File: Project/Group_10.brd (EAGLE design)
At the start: 73.7 x 48.3 mm, 29 parts, among them J1 POWER_JACKPTH_LOCK, U1 +12v, U3 TCA9546ASO16, U4 TMUX1208

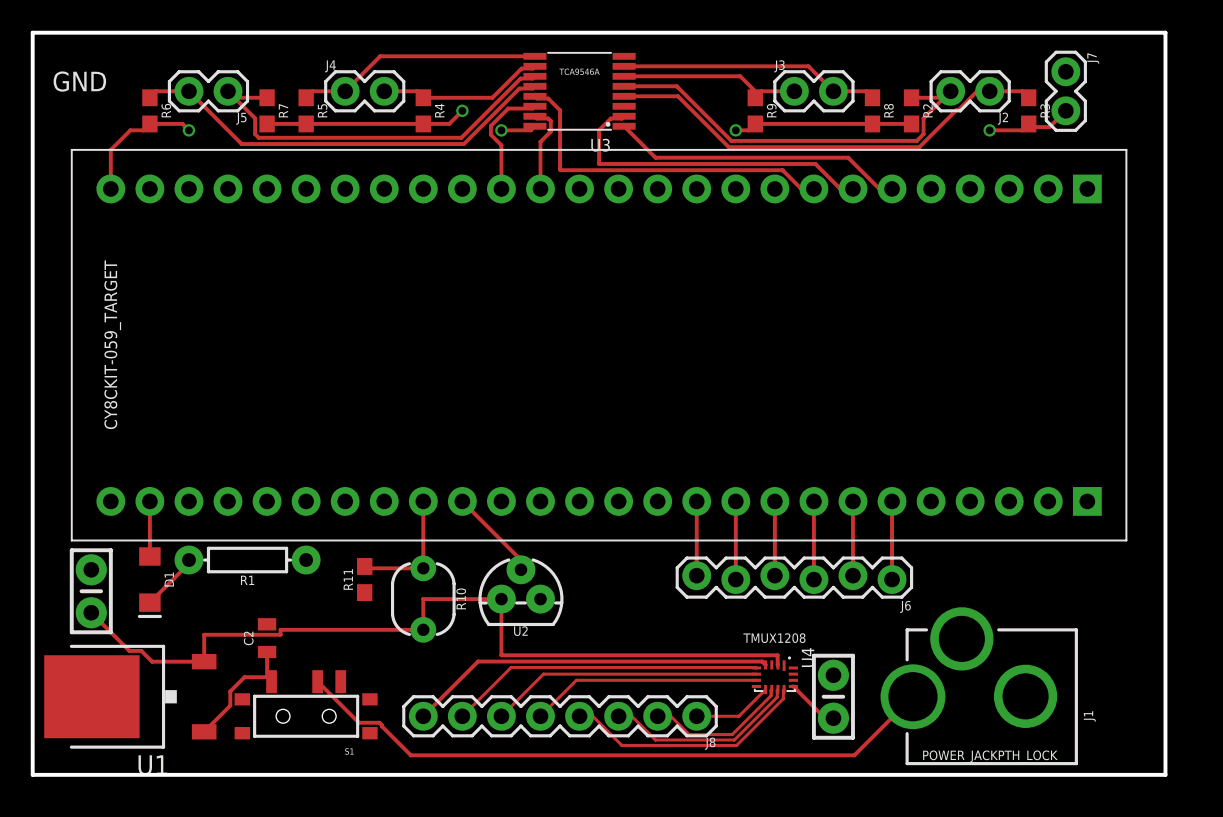
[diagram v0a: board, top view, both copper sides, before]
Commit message: Updated devices on board, corrected isolate of copper pour, simplified some routing
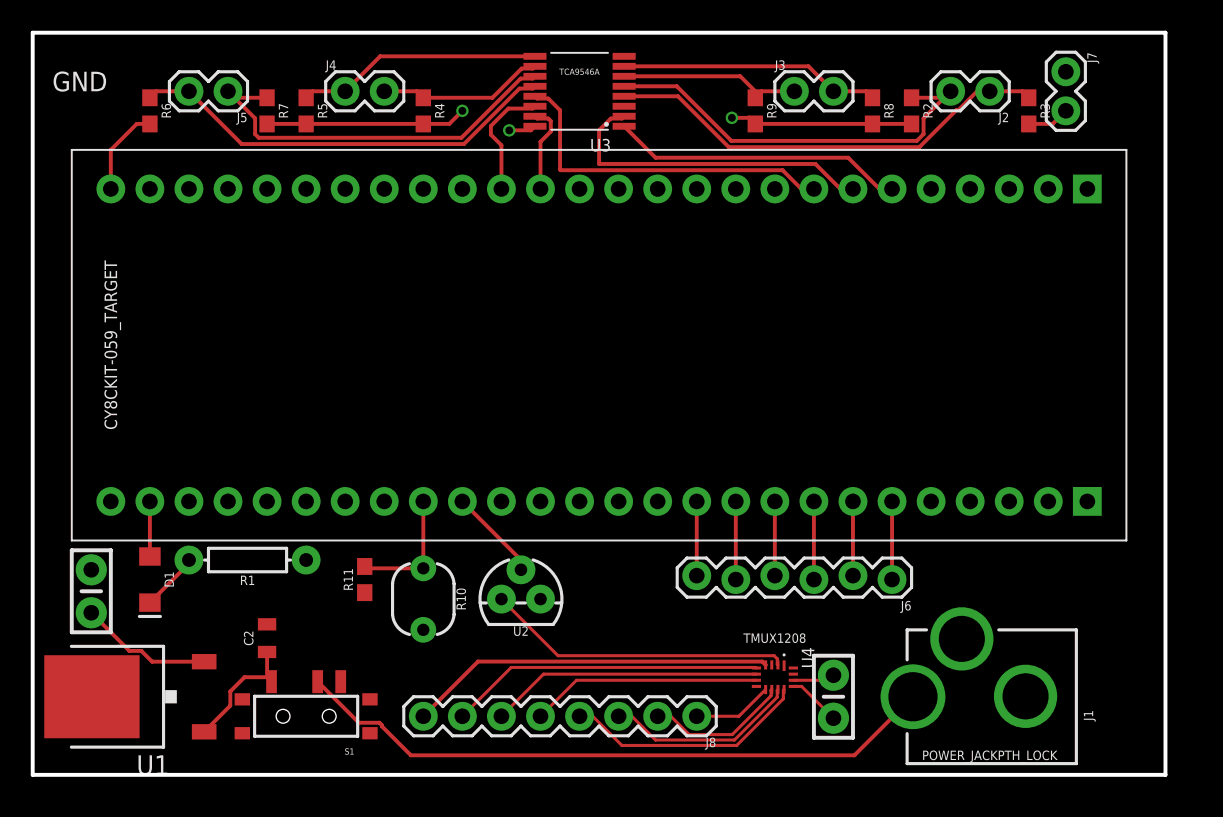
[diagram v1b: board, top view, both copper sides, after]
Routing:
- net 5V: track 99.0 -> 67.3 mm, vias 5 -> 3
- net GND: track 0.00 -> 2.75 mm
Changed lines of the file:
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@@
 <setting verticaltext="up"/>
 </settings>
-<grid distance="0.05" unitdist="inch" unit="mil" style="lines" multiple="1" display="yes" altdistance="0.005" altunitdist="inch" altunit="inch"/>
+<grid distance="2" unitdist="mil" unit="mil" style="lines" multiple="1" display="yes" altdistance="2" altunitdist="mil" altunit="mil"/>
 <layers>
 <layer number="1" name="Top" color="4" fill="1" visible="yes" active="yes"/>
@@
 <layer number="23" name="tOrigins" color="15" fill="1" visible="yes" active="yes"/>
 <layer number="24" name="bOrigins" color="15" fill="1" visible="yes" active="yes"/>
-<layer number="25" name="tNames" color="7" fill="1" visible="no" active="yes"/>
+<layer number="25" name="tNames" color="7" fill="1" visible="yes" active="yes"/>
 <layer number="26" name="bNames" color="7" fill="1" visible="no" active="yes"/>
-<layer number="27" name="tValues" color="7" fill="1" visible="no" active="yes"/>
+<layer number="27" name="tValues" color="7" fill="1" visible="yes" active="yes"/>
 <layer number="28" name="bValues" color="7" fill="1" visible="no" active="yes"/>
 <layer number="29" name="tStop" color="7" fill="3" visible="no" active="yes"/>
@@
 </class>
 </classes>
-<designrules name="Group_10">
+<designrules name="Group_10 *">
 <description language="en">Design rules from &lt;a href=&quot;https://www.mdsrl.it/&quot;&gt;MD srl&lt;/a&gt;</description>
 <param name="layerSetup" value="(1*16)"/>
@@
 <contactref element="U3" pad="3"/>
 <contactref element="U3" pad="8"/>
-<polygon width="0.254" layer="1">
+<polygon width="0.254" layer="1" isolate="0.2032">
 <vertex x="-74.93" y="45.72"/>
 <vertex x="-74.93" y="93.98"/>
@@
 <vertex x="-1.27" y="45.72"/>
 </polygon>
+<wire x1="-25.47" y1="51.87" x2="-23.187" y2="51.87" width="0.2" layer="1"/>
+<wire x1="-23.187" y1="51.87" x2="-22.86" y2="52.197" width="0.2" layer="1"/>
 </signal>
 <signal name="12V">
@@
 <contactref element="U3" pad="16"/>
 <wire x1="-42.27" y1="87.895" x2="-42.535" y2="87.63" width="0.254" layer="1"/>
-<wire x1="-42.535" y1="87.63" x2="-44.45" y2="87.63" width="0.254" layer="1"/>
-<via x="-44.45" y="87.63" extent="1-16" drill="0.508"/>
+<wire x1="-42.535" y1="87.63" x2="-43.942" y2="87.63" width="0.254" layer="1"/>
+<via x="-43.942" y="87.63" extent="1-16" drill="0.508"/>
 <wire x1="-59.69" y1="88.05" x2="-57.15" y2="88.05" width="0.254" layer="1"/>
-<wire x1="-67.31" y1="88.05" x2="-65.19" y2="88.05" width="0.254" layer="1"/>
-<wire x1="-65.19" y1="88.05" x2="-64.77" y2="87.63" width="0.254" layer="1"/>
-<via x="-64.77" y="87.63" extent="1-16" drill="0.508"/>
 <wire x1="-57.15" y1="88.05" x2="-49.53" y2="88.05" width="0.254" layer="1"/>
 <wire x1="-49.53" y1="88.05" x2="-47.84" y2="88.05" width="0.254" layer="1"/>
 <wire x1="-47.84" y1="88.05" x2="-46.99" y2="88.9" width="0.254" layer="1"/>
 <via x="-46.99" y="88.9" extent="1-16" drill="0.508"/>
-<wire x1="-67.31" y1="88.05" x2="-67.73" y2="87.63" width="0.254" layer="1"/>
-<wire x1="-67.73" y1="87.63" x2="-68.58" y2="87.63" width="0.254" layer="1"/>
-<wire x1="-68.58" y1="87.63" x2="-69.85" y2="86.36" width="0.254" layer="1"/>
-<wire x1="-69.85" y1="86.36" x2="-69.85" y2="83.82" width="0.254" layer="1"/>
-<wire x1="-27.94" y1="88.05" x2="-28.36" y2="87.63" width="0.254" layer="1"/>
-<wire x1="-28.36" y1="87.63" x2="-29.21" y2="87.63" width="0.254" layer="1"/>
-<via x="-29.21" y="87.63" extent="1-16" drill="0.508"/>
+<wire x1="-69.85" y1="83.82" x2="-69.85" y2="86.36" width="0.254" layer="1"/>
+<wire x1="-27.94" y1="88.05" x2="-28.3328" y2="88.4428" width="0.254" layer="1"/>
+<wire x1="-28.3328" y1="88.4428" x2="-29.464" y2="88.4428" width="0.254" layer="1"/>
+<via x="-29.464" y="88.4428" extent="1-16" drill="0.508"/>
 <wire x1="-27.94" y1="88.05" x2="-20.32" y2="88.05" width="0.254" layer="1"/>
 <wire x1="-20.32" y1="88.05" x2="-17.78" y2="88.05" width="0.254" layer="1"/>
-<wire x1="-10.16" y1="88.05" x2="-10.37" y2="87.84" width="0.254" layer="1"/>
-<wire x1="-10.37" y1="87.84" x2="-10.58" y2="87.63" width="0.254" layer="1"/>
-<wire x1="-10.58" y1="87.63" x2="-12.7" y2="87.63" width="0.254" layer="1"/>
-<via x="-12.7" y="87.63" extent="1-16" drill="0.508"/>
-<wire x1="-7.747" y1="88.9" x2="-8.807" y2="87.84" width="0.254" layer="1"/>
-<wire x1="-8.807" y1="87.84" x2="-10.37" y2="87.84" width="0.254" layer="1"/>
-<wire x1="-25.47" y1="51.47" x2="-23.403" y2="49.403" width="0.254" layer="1"/>
-<wire x1="-23.403" y1="49.403" x2="-22.86" y2="49.403" width="0.254" layer="1"/>
 <wire x1="-71.12" y1="56.261" x2="-68.6384" y2="53.7794" width="0.254" layer="1"/>
 <wire x1="-68.6384" y1="53.7794" x2="-67.86426875" y2="53.7794" width="0.254" layer="1"/>
 <wire x1="-67.16486875" y1="53.08" x2="-63.78" y2="53.08" width="0.254" layer="1"/>
 <wire x1="-67.86426875" y1="53.7794" x2="-67.16486875" y2="53.08" width="0.254" layer="1"/>
-<wire x1="-26.47" y1="52.87" x2="-26.4906" y2="52.87" width="0.254" layer="1"/>
-<wire x1="-44.45" y1="53.4956" x2="-44.45" y2="57.15" width="0.254" layer="1"/>
-<wire x1="-26.4906" y1="52.87" x2="-26.4906" y2="53.4956" width="0.254" layer="1"/>
-<wire x1="-26.4906" y1="53.4956" x2="-44.45" y2="53.4956" width="0.254" layer="1"/>
-<wire x1="-44.45" y1="57.15" x2="-49.53" y2="57.15" width="0.254" layer="1"/>
-<wire x1="-49.53" y1="57.15" x2="-49.53" y2="55.15" width="0.254" layer="1"/>
-<wire x1="-58.8106" y1="54.8306" x2="-58.8106" y2="55.15" width="0.254" layer="1"/>
-<wire x1="-58.8106" y1="55.15" x2="-49.53" y2="55.15" width="0.254" layer="1"/>
-<wire x1="-63.78" y1="53.08" x2="-63.78" y2="54.8306" width="0.254" layer="1"/>
-<wire x1="-63.78" y1="54.8306" x2="-58.8106" y2="54.8306" width="0.254" layer="1"/>
-<polygon width="0.254" layer="16">
+<polygon width="0.254" layer="16" isolate="0.2032">
 <vertex x="-74.93" y="45.72"/>
 <vertex x="-74.93" y="93.98"/>
@@
 <vertex x="-1.27" y="45.72"/>
 </polygon>
+<wire x1="-25.47" y1="51.47" x2="-24.927" y2="51.47" width="0.2" layer="1"/>
+<wire x1="-24.927" y1="51.47" x2="-22.86" y2="49.403" width="0.2" layer="1"/>
+<wire x1="-44.45" y1="57.15" x2="-40.7686" y2="53.4686" width="0.2" layer="1"/>
+<wire x1="-26.5176" y1="53.27455" x2="-26.5176" y2="52.9176" width="0.2" layer="1"/>
+<wire x1="-26.5176" y1="52.9176" x2="-26.47" y2="52.87" width="0.2" layer="1"/>
+<wire x1="-40.7686" y1="53.4686" x2="-26.71165" y2="53.4686" width="0.2" layer="1"/>
+<wire x1="-26.71165" y1="53.4686" x2="-26.5176" y2="53.27455" width="0.2" layer="1"/>
+<wire x1="-68.16" y1="88.05" x2="-67.31" y2="88.05" width="0.254" layer="1"/>
+<wire x1="-69.85" y1="86.36" x2="-68.16" y2="88.05" width="0.254" layer="1"/>
+<wire x1="-10.16" y1="88.05" x2="-8.597" y2="88.05" width="0.254" layer="1"/>
+<wire x1="-8.597" y1="88.05" x2="-7.747" y2="88.9" width="0.254" layer="1"/>
 </signal>
 <signal name="PHOTO_OUT">

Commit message: Corrected silkscreen font width to match manifacturer's, added some information and corrected some routing
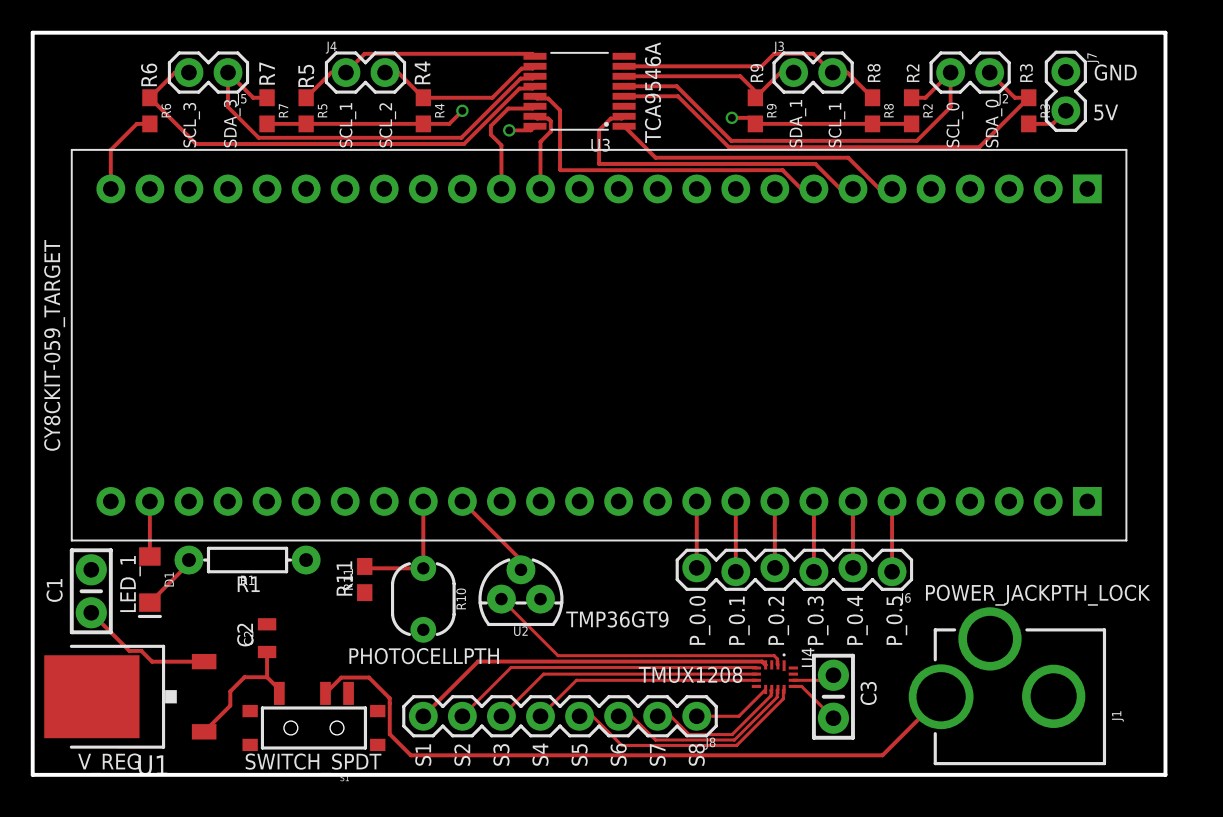
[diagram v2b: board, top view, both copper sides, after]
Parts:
- moved J1 1.83 mm to (-1.98, 50.8)
- moved J3 1.22 mm to (-25.5, 91.4)
- moved J4 1.22 mm to (-54.6, 91.4)
- moved J2 1.22 mm to (-12.7, 91.4)
- moved J5 1.22 mm to (-62.2, 91.4)
- moved S1 0.92 mm to (-56.6, 48.8)
- moved J6 0.51 mm to (-19.1, 58.9)
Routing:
- net N$1: track 42.3 -> 45.5 mm
- net I2C_SDA_0: track 29.4 -> 32.2 mm
- net I2C_SCL_3: track 28.2 -> 31.1 mm
- net I2C_SDA_3: track 26.2 -> 27.9 mm
- net I2C_SCL_0: track 27.4 -> 29.1 mm
- net 12V: track 8.15 -> 9.12 mm
- net I2C_SCL_1: track 17.0 -> 17.7 mm
- net N$9: track 4.83 -> 4.32 mm
- net N$7: track 4.83 -> 4.32 mm
- net N$5: track 4.83 -> 4.32 mm
- net N$8: track 5.08 -> 4.57 mm
- net N$6: track 5.08 -> 4.57 mm
- net N$4: track 5.08 -> 4.57 mm
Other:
- board text added: "C1"
- board text added: "C2"
- board text added: "C3"
- board text added: "LED_1"
- board text added: "PHOTOCELLPTH"
- board text added: "P_0.0"
- board text added: "P_0.1"
- board text added: "P_0.2"
- board text added: "P_0.3"
- board text added: "P_0.4"
- board text added: "P_0.5"
- board text added: "R1"
- board text added: "R11"
- board text added: "R2"
- board text added: "R3"
- board text added: "R4"
- board text added: "R5"
- board text added: "R6"
- board text added: "R7"
- board text added: "R8"
- board text added: "R9"
- board text added: "S1"
- board text added: "S2"
- board text added: "S3"
- board text added: "S4"
- board text added: "S5"
- board text added: "S6"
- board text added: "S7"
- board text added: "S8"
- board text added: "SCL_0"
- board text added: "SCL_1"
- board text added: "SCL_2"
- board text added: "SCL_3"
- board text added: "SDA_0"
- board text added: "SDA_1"
- board text added: "SDA_3"
- board text added: "SWITCH_SPDT"
- board text added: "TMP36GT9"
- board text added: "V_REG"
